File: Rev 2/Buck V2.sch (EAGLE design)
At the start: 51 parts, among them Q1 IRF3205STRLPBF, Q2 IRF3205STRLPBF, Q3 IRF3205STRLPBF, Q4 IRF3205STRLPBF, U1 Value

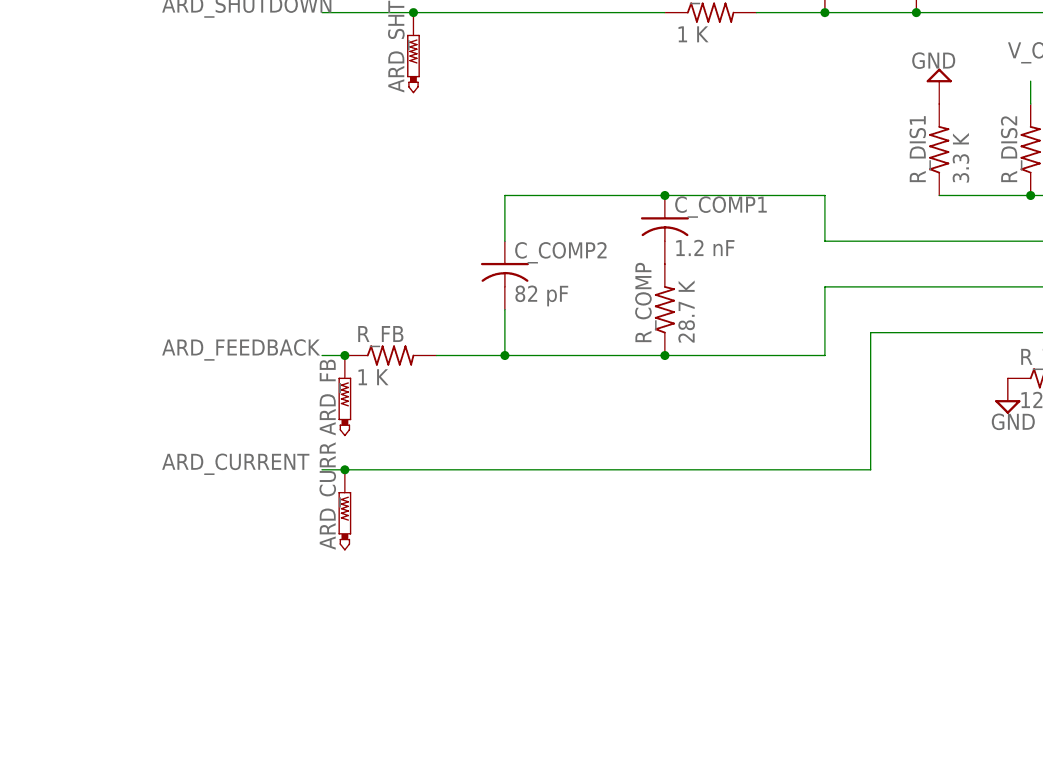
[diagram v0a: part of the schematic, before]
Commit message: Finished evreything, boards ordered from JLC! Hi Thomas
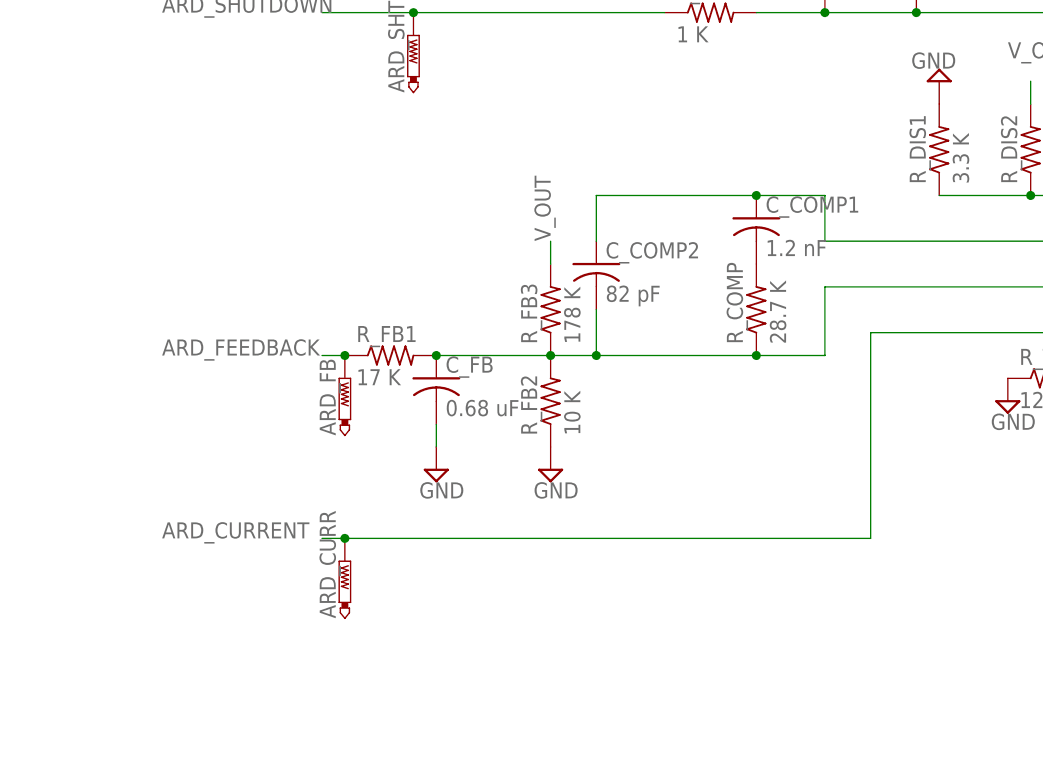
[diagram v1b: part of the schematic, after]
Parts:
- added C_FB: 0.68 uF, rcl:C-USC0603
- added R_FB2: 10 K, rcl:R-US_R0603
- added R_FB3: 178 K, rcl:R-US_R0603
- R_FB1: value 1 K -> 17 K
- renumbered R_FB to R_FB1
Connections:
- net GND: now also C_FB.2, R_FB2.1
- net N$15: now also C_FB.1, R_FB2.2, R_FB3.1
- net V_OUT: now also R_FB3.2
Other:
- moved on the sheet: ARD_CURR, C_COMP1, C_COMP2, R_COMP
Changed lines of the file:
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@@
 <part name="C_COMP2" library="rcl" deviceset="C-US" device="C0603" value="82 pF"/>
 <part name="R_COMP" library="rcl" deviceset="R-US_" device="R0603" value="28.7 K"/>
-<part name="R_FB" library="rcl" deviceset="R-US_" device="R0603" value="1 K"/>
+<part name="R_FB1" library="rcl" deviceset="R-US_" device="R0603" value="17 K"/>
 <part name="R_T" library="rcl" deviceset="R-US_" device="R0603" value="12.1 K"/>
 <part name="SUPPLY8" library="supply2" deviceset="GND" device=""/>
@@
 <part name="LO" library="testpad" deviceset="PTR1" device="TP20R"/>
 <part name="CURR_SENSE" library="testpad" deviceset="PTR1" device="TP20R"/>
+<part name="R_FB2" library="rcl" deviceset="R-US_" device="R0603" value="10 K"/>
+<part name="R_FB3" library="rcl" deviceset="R-US_" device="R0603" value="178 K"/>
+<part name="SUPPLY14" library="supply2" deviceset="GND" device=""/>
+<part name="C_FB" library="rcl" deviceset="C-US" device="C0603" value="0.68 uF"/>
+<part name="SUPPLY15" library="supply2" deviceset="GND" device=""/>
 </parts>
 <sheets>
@@
 <attribute name="VALUE" x="-3.175" y="84.455" size="1.778" layer="96" rot="R180"/>
 </instance>
-<instance part="C_COMP1" gate="G$1" x="-35.56" y="66.04" smashed="yes">
-<attribute name="NAME" x="-34.544" y="66.675" size="1.778" layer="95"/>
-<attribute name="VALUE" x="-34.544" y="61.849" size="1.778" layer="96"/>
-</instance>
-<instance part="C_COMP2" gate="G$1" x="-53.34" y="60.96" smashed="yes">
-<attribute name="NAME" x="-52.324" y="61.595" size="1.778" layer="95"/>
-<attribute name="VALUE" x="-52.324" y="56.769" size="1.778" layer="96"/>
-</instance>
-<instance part="R_COMP" gate="G$1" x="-35.56" y="55.88" smashed="yes" rot="R90">
-<attribute name="NAME" x="-37.0586" y="52.07" size="1.778" layer="95" rot="R90"/>
-<attribute name="VALUE" x="-32.258" y="52.07" size="1.778" layer="96" rot="R90"/>
-</instance>
-<instance part="R_FB" gate="G$1" x="-66.04" y="50.8" smashed="yes">
+<instance part="C_COMP1" gate="G$1" x="-25.4" y="66.04" smashed="yes">
+<attribute name="NAME" x="-24.384" y="66.675" size="1.778" layer="95"/>
+<attribute name="VALUE" x="-24.384" y="61.849" size="1.778" layer="96"/>
+</instance>
+<instance part="C_COMP2" gate="G$1" x="-43.18" y="60.96" smashed="yes">
+<attribute name="NAME" x="-42.164" y="61.595" size="1.778" layer="95"/>
+<attribute name="VALUE" x="-42.164" y="56.769" size="1.778" layer="96"/>
+</instance>
+<instance part="R_COMP" gate="G$1" x="-25.4" y="55.88" smashed="yes" rot="R90">
+<attribute name="NAME" x="-26.8986" y="52.07" size="1.778" layer="95" rot="R90"/>
+<attribute name="VALUE" x="-22.098" y="52.07" size="1.778" layer="96" rot="R90"/>
+</instance>
+<instance part="R_FB1" gate="G$1" x="-66.04" y="50.8" smashed="yes">
 <attribute name="NAME" x="-69.85" y="52.2986" size="1.778" layer="95"/>
 <attribute name="VALUE" x="-69.85" y="47.498" size="1.778" layer="96"/>
@@
 <attribute name="TP_SIGNAL_NAME" x="-69.85" y="45.72" size="1.778" layer="97"/>
 </instance>
-<instance part="ARD_CURR" gate="G$1" x="-71.12" y="35.56" smashed="yes">
-<attribute name="NAME" x="-72.136" y="29.21" size="1.778" layer="95" rot="R90"/>
-<attribute name="TP_SIGNAL_NAME" x="-69.85" y="33.02" size="1.778" layer="97"/>
+<instance part="ARD_CURR" gate="G$1" x="-71.12" y="27.94" smashed="yes">
+<attribute name="NAME" x="-72.136" y="21.59" size="1.778" layer="95" rot="R90"/>
+<attribute name="TP_SIGNAL_NAME" x="-69.85" y="25.4" size="1.778" layer="97"/>
 </instance>
 <instance part="VCC" gate="G$1" x="147.32" y="76.2" smashed="yes">
@@
 <attribute name="NAME" x="189.484" y="29.21" size="1.778" layer="95" rot="R90"/>
 <attribute name="TP_SIGNAL_NAME" x="191.77" y="33.02" size="1.778" layer="97"/>
+</instance>
+<instance part="R_FB2" gate="G$1" x="-48.26" y="45.72" smashed="yes" rot="R90">
+<attribute name="NAME" x="-49.7586" y="41.91" size="1.778" layer="95" rot="R90"/>
+<attribute name="VALUE" x="-44.958" y="41.91" size="1.778" layer="96" rot="R90"/>
+</instance>
+<instance part="R_FB3" gate="G$1" x="-48.26" y="55.88" smashed="yes" rot="R90">
+<attribute name="NAME" x="-49.7586" y="52.07" size="1.778" layer="95" rot="R90"/>
+<attribute name="VALUE" x="-44.958" y="52.07" size="1.778" layer="96" rot="R90"/>
+</instance>
+<instance part="SUPPLY14" gate="GND" x="-48.26" y="38.1" smashed="yes">
+<attribute name="VALUE" x="-50.165" y="34.925" size="1.778" layer="96"/>
+</instance>
+<instance part="C_FB" gate="G$1" x="-60.96" y="48.26" smashed="yes">
+<attribute name="NAME" x="-59.944" y="48.895" size="1.778" layer="95"/>
+<attribute name="VALUE" x="-59.944" y="44.069" size="1.778" layer="96"/>
+</instance>
+<instance part="SUPPLY15" gate="GND" x="-60.96" y="38.1" smashed="yes">
+<attribute name="VALUE" x="-62.865" y="34.925" size="1.778" layer="96"/>
 </instance>
 </instances>
@@
 <label x="284.48" y="96.52" size="1.778" layer="95"/>
 </segment>
+<segment>
+<pinref part="R_FB2" gate="G$1" pin="1"/>
+<pinref part="SUPPLY14" gate="GND" pin="GND"/>
+</segment>
+<segment>
+<pinref part="C_FB" gate="G$1" pin="2"/>
+<pinref part="SUPPLY15" gate="GND" pin="GND"/>
+<wire x1="-60.96" y1="43.18" x2="-60.96" y2="40.64" width="0.1524" layer="91"/>
+</segment>
 </net>
 <net name="N$5" class="0">
@@
 <label x="2.54" y="83.82" size="1.778" layer="95"/>
 </segment>
+<segment>
+<pinref part="R_FB3" gate="G$1" pin="2"/>
+<wire x1="-48.26" y1="60.96" x2="-48.26" y2="63.5" width="0.1524" layer="91"/>
+<label x="-48.26" y="63.5" size="1.778" layer="95" rot="R90"/>
+</segment>
 </net>
 <net name="N$7" class="0">
@@
 <pinref part="C_COMP2" gate="G$1" pin="1"/>
 <pinref part="C_COMP1" gate="G$1" pin="1"/>
-<wire x1="-53.34" y1="63.5" x2="-53.34" y2="68.58" width="0.1524" layer="91"/>
-<wire x1="-53.34" y1="68.58" x2="-35.56" y2="68.58" width="0.1524" layer="91"/>
-<junction x="-35.56" y="68.58"/>
-<wire x1="-35.56" y1="68.58" x2="-17.78" y2="68.58" width="0.1524" layer="91"/>
+<wire x1="-43.18" y1="63.5" x2="-43.18" y2="68.58" width="0.1524" layer="91"/>
+<wire x1="-43.18" y1="68.58" x2="-25.4" y2="68.58" width="0.1524" layer="91"/>
+<junction x="-25.4" y="68.58"/>
+<wire x1="-25.4" y1="68.58" x2="-17.78" y2="68.58" width="0.1524" layer="91"/>
 <wire x1="-17.78" y1="68.58" x2="-17.78" y2="63.5" width="0.1524" layer="91"/>
 <pinref part="U1" gate="A" pin="COMP"/>
@@
 <segment>
 <pinref part="C_COMP2" gate="G$1" pin="2"/>
-<wire x1="-53.34" y1="55.88" x2="-53.34" y2="50.8" width="0.1524" layer="91"/>
+<wire x1="-43.18" y1="55.88" x2="-43.18" y2="50.8" width="0.1524" layer="91"/>
 <pinref part="R_COMP" gate="G$1" pin="1"/>
-<wire x1="-53.34" y1="50.8" x2="-35.56" y2="50.8" width="0.1524" layer="91"/>
-<wire x1="-35.56" y1="50.8" x2="-17.78" y2="50.8" width="0.1524" layer="91"/>
+<wire x1="-43.18" y1="50.8" x2="-25.4" y2="50.8" width="0.1524" layer="91"/>
+<wire x1="-25.4" y1="50.8" x2="-17.78" y2="50.8" width="0.1524" layer="91"/>
 <wire x1="-17.78" y1="50.8" x2="-17.78" y2="58.42" width="0.1524" layer="91"/>
-<junction x="-35.56" y="50.8"/>
+<junction x="-25.4" y="50.8"/>
 <pinref part="U1" gate="A" pin="FB"/>
 <wire x1="-17.78" y1="58.42" x2="53.34" y2="58.42" width="0.1524" layer="91"/>
-<pinref part="R_FB" gate="G$1" pin="2"/>
-<wire x1="-60.96" y1="50.8" x2="-53.34" y2="50.8" width="0.1524" layer="91"/>
-<junction x="-53.34" y="50.8"/>
+<pinref part="R_FB1" gate="G$1" pin="2"/>
+<wire x1="-60.96" y1="50.8" x2="-48.26" y2="50.8" width="0.1524" layer="91"/>
+<junction x="-43.18" y="50.8"/>
+<pinref part="R_FB2" gate="G$1" pin="2"/>
+<wire x1="-48.26" y1="50.8" x2="-43.18" y2="50.8" width="0.1524" layer="91"/>
+<junction x="-48.26" y="50.8"/>
+<pinref part="R_FB3" gate="G$1" pin="1"/>
+<pinref part="C_FB" gate="G$1" pin="1"/>
+<junction x="-60.96" y="50.8"/>
 </segment>
 </net>
 <net name="ARD_FEEDBACK" class="0">
 <segment>
-<pinref part="R_FB" gate="G$1" pin="1"/>
+<pinref part="R_FB1" gate="G$1" pin="1"/>
 <wire x1="-71.12" y1="50.8" x2="-73.66" y2="50.8" width="0.1524" layer="91"/>
 <label x="-91.44" y="50.8" size="1.778" layer="95"/>
@@
 <pinref part="U1" gate="A" pin="CM"/>
 <wire x1="53.34" y1="53.34" x2="-12.7" y2="53.34" width="0.1524" layer="91"/>
-<wire x1="-12.7" y1="53.34" x2="-12.7" y2="38.1" width="0.1524" layer="91"/>
-<wire x1="-12.7" y1="38.1" x2="-71.12" y2="38.1" width="0.1524" layer="91"/>
-<label x="-91.44" y="38.1" size="1.778" layer="95"/>
+<wire x1="-12.7" y1="53.34" x2="-12.7" y2="30.48" width="0.1524" layer="91"/>
+<wire x1="-12.7" y1="30.48" x2="-71.12" y2="30.48" width="0.1524" layer="91"/>
+<label x="-91.44" y="30.48" size="1.778" layer="95"/>
 <pinref part="ARD_CURR" gate="G$1" pin="TP"/>
-<wire x1="-71.12" y1="38.1" x2="-73.66" y2="38.1" width="0.1524" layer="91"/>
-<junction x="-71.12" y="38.1"/>
-</segment>
-<segment>
+<wire x1="-71.12" y1="30.48" x2="-73.66" y2="30.48" width="0.1524" layer="91"/>
+<junction x="-71.12" y="30.48"/>
+</segment>
+<segment>
